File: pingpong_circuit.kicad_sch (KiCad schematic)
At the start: 10 parts, among them J1 XH, SW1 PA, SW2 PA, U1 Pico, U2 A000053

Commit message: hoge
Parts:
- added J2: Brushless, symbol Connector:Conn_01x02_Pin
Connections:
- net at U1.4 (GPIO2): now also J2.2 (Pin_2)
- net at U1.5 (GPIO3): now also J2.1 (Pin_1)
- no-connect marks 1 -> 3
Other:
- note added: "servo?"
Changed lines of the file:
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@@
 	(generator_version "9.0")
 	(paper "A4")
+	(text "servo?"
+		(exclude_from_sim no)
+		(at 100.33 61.722 0)
+		(effects
+			(font
+				(size 1.27 1.27)
+			)
+		)
+	)
 	(text "赤\n青\n緑\n黒"
 		(exclude_from_sim no)
@@
 	)
 	(no_connect
+		(at 55.88 31.75)
+	)
+	(no_connect
+		(at 55.88 41.91)
+	)
+	(no_connect
 		(at 228.6 46.99)
 	)
@@
 	(wire
 		(pts
+			(xy 92.71 52.07) (xy 92.71 66.04)
+		)
+		(stroke
+			(width 0)
+			(type default)
+		)
+	)
+	(wire
+		(pts
 			(xy 228.6 52.07) (xy 223.52 52.07)
 		)
@@
 	(wire
 		(pts
+			(xy 97.79 55.88) (xy 97.79 39.37)
+		)
+		(stroke
+			(width 0)
+			(type default)
+		)
+	)
+	(wire
+		(pts
 			(xy 132.08 80.01) (xy 123.19 80.01)
 		)
@@
 	(wire
 		(pts
+			(xy 55.88 44.45) (xy 95.25 44.45)
+		)
+		(stroke
+			(width 0)
+			(type default)
+		)
+	)
+	(wire
+		(pts
 			(xy 123.19 68.58) (xy 123.19 64.77)
 		)
@@
 	(wire
 		(pts
+			(xy 95.25 44.45) (xy 95.25 63.5)
+		)
+		(stroke
+			(width 0)
+			(type default)
+		)
+	)
+	(wire
+		(pts
 			(xy 251.46 57.15) (xy 264.16 57.15)
 		)
@@
 	(wire
 		(pts
+			(xy 100.33 53.34) (xy 109.22 53.34)
+		)
+		(stroke
+			(width 0)
+			(type default)
+		)
+	)
+	(wire
+		(pts
 			(xy 157.48 67.31) (xy 157.48 93.98)
 		)
@@
 	(wire
 		(pts
+			(xy 55.88 52.07) (xy 92.71 52.07)
+		)
+		(stroke
+			(width 0)
+			(type default)
+		)
+	)
+	(wire
+		(pts
+			(xy 95.25 63.5) (xy 100.33 63.5)
+		)
+		(stroke
+			(width 0)
+			(type default)
+		)
+	)
+	(wire
+		(pts
 			(xy 16.51 29.21) (xy 20.32 29.21)
 		)
@@
 	(wire
 		(pts
+			(xy 55.88 36.83) (xy 100.33 36.83)
+		)
+		(stroke
+			(width 0)
+			(type default)
+		)
+	)
+	(wire
+		(pts
 			(xy 219.71 62.23) (xy 228.6 62.23)
 		)
@@
 	(wire
 		(pts
+			(xy 92.71 66.04) (xy 100.33 66.04)
+		)
+		(stroke
+			(width 0)
+			(type default)
+		)
+	)
+	(wire
+		(pts
 			(xy 228.6 57.15) (xy 228.6 59.69)
 		)
@@
 	(wire
 		(pts
+			(xy 109.22 55.88) (xy 97.79 55.88)
+		)
+		(stroke
+			(width 0)
+			(type default)
+		)
+	)
+	(wire
+		(pts
 			(xy 140.97 43.18) (xy 140.97 34.29)
 		)
@@
 	(wire
 		(pts
+			(xy 100.33 36.83) (xy 100.33 53.34)
+		)
+		(stroke
+			(width 0)
+			(type default)
+		)
+	)
+	(wire
+		(pts
 			(xy 228.6 64.77) (xy 222.25 64.77)
+		)
+		(stroke
+			(width 0)
+			(type default)
+		)
+	)
+	(wire
+		(pts
+			(xy 97.79 39.37) (xy 55.88 39.37)
 		)
 		(stroke
@@
 					(unit 1)
 				)
+			)
+		)
+	)
+	(symbol
+		(lib_id "Connector:Conn_01x02_Pin")
+		(at 114.3 55.88 180)
+		(unit 1)
+		(exclude_from_sim no)
+		(in_bom yes)
+		(on_board yes)
+		(dnp no)
+		(fields_autoplaced yes)
+		(property "Reference" "J2"
+			(at 115.57 53.3399 0)
+			(effects
+				(font
+					(size 1.27 1.27)
+				)
+				(justify right)
+			)
+		)
+		(property "Value" "Brushless"
+			(at 115.57 55.8799 0)
+			(effects
+				(font
+					(size 1.27 1.27)
+				)
+				(justify right)
+			)
+		)
+		(property "Footprint" ""
+			(at 114.3 55.88 0)
+			(effects
+				(font
+					(size 1.27 1.27)
+				)
+				(hide yes)
+			)
+		)
+		(property "Datasheet" "~"
+			(at 114.3 55.88 0)
+			(effects
+				(font
+					(size 1.27 1.27)
+				)
+				(hide yes)
+			)
+		)
+		(property "Description" "Generic connector, single row, 01x02, script generated"
+			(at 114.3 55.88 0)
+			(effects
+				(font
+					(size 1.27 1.27)
+				)
+				(hide yes)
+			)
+		)
+		(pin "1"
+		)
+		(pin "2"
+		)
+		(instances
+			(project ""
+				(path "/fc07d479-f2e9-4808-b332-bbe7c10248ce"
+					(reference "J2")
+					(unit 1)
+				)

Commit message: 一旦全体像把握
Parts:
- removed J2: Brushless, symbol Connector:Conn_01x02_Pin
- added C3: 470u, symbol Device:C_Polarized
- added C4, C5: C_Polarized, symbol Device:C_Polarized
- added J10: QI_3, symbol Connector:Conn_01x03_Pin
- added J2: QI_Servo_Roll, symbol Connector:Conn_01x03_Pin
- added J3: QI_Blushless_Left, symbol Connector:Conn_01x03_Pin
- added J4: QI_Blushless_Right, symbol Connector:Conn_01x03_Pin
- added J5: QI_Servo_Pitch, symbol Connector:Conn_01x03_Pin
- added J6: QI_Servo_Yaw, symbol Connector:Conn_01x03_Pin
- added J7: QI_Servo_Loading, symbol Connector:Conn_01x03_Pin
- added J8: Arduino_Uno_UART, symbol Connector:Conn_01x04_Pin
- added J9: XT60, symbol Connector_Generic:Conn_01x02
- U3: value ~ -> A4988
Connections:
- net +5V: now also J8.4 (Pin_4)
- net GND: now also U1.13 (GND), U1.18 (GND), U1.23 (GND), U1.28 (GND), U1.33 (AGND), U1.38 (GND), U1.8 (GND), C3.2, C4.2, C5.2, J10.2 (Pin_2), J2.1 (Pin_1), J3.1 (Pin_1), J4.1 (Pin_1), J5.1 (Pin_1), J6.1 (Pin_1), J7.1 (Pin_1), J8.1 (Pin_1), J9.1 (Pin_1); no longer U3.2 (MS1), U3.3 (MS2), U3.4 (MS3)
- net at U3.1 (~{ENABLE}): now also U2.12 (7)
- net at U3.5 (~{RESET}), U3.6 (~{SLEEP}): now also U2.18 (13(PWM))
- net at U2.15 (10(PWM)/A10): now also U3.2 (MS1)
- net at U2.16 (11(PWM)): now also U3.3 (MS2)
- net at U2.17 (12/A11): now also U3.4 (MS3)
- net at U2.3 (1/TX): now also U1.21 (GPIO16)
- net at U2.4 (0/RX): now also U1.22 (GPIO17); no longer U1.1 (GPIO0)
- net at U1.5 (GPIO3): now also J5.3 (Pin_3)
- net at U1.4 (GPIO2): now also J2.3 (Pin_3)
- net at U1.15 (GPIO11): now also J8.3 (Pin_3)
- net at U1.16 (GPIO12): now also J8.2 (Pin_2)
- net at U1.2 (GPIO1): now also J4.3 (Pin_3)
- net at U1.7 (GPIO5): now also J6.3 (Pin_3)
- net at U1.9 (GPIO6): now also J7.3 (Pin_3)
- net +24V renamed +15V
- net +15V: now also C3.1, C4.1, J9.2 (Pin_2)
- new net: J3.3 (Pin_3), U1.1 (GPIO0)
- new net +7.5V: C5.1, J10.1 (Pin_1), J2.2 (Pin_2), J5.2 (Pin_2), J6.2 (Pin_2), J7.2 (Pin_2)
- no-connect marks 3 -> 44
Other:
- note removed: "servo?"
- moved on the sheet: C1, C2, J1, R1, R2, SW1, SW2, U1, U2, U3

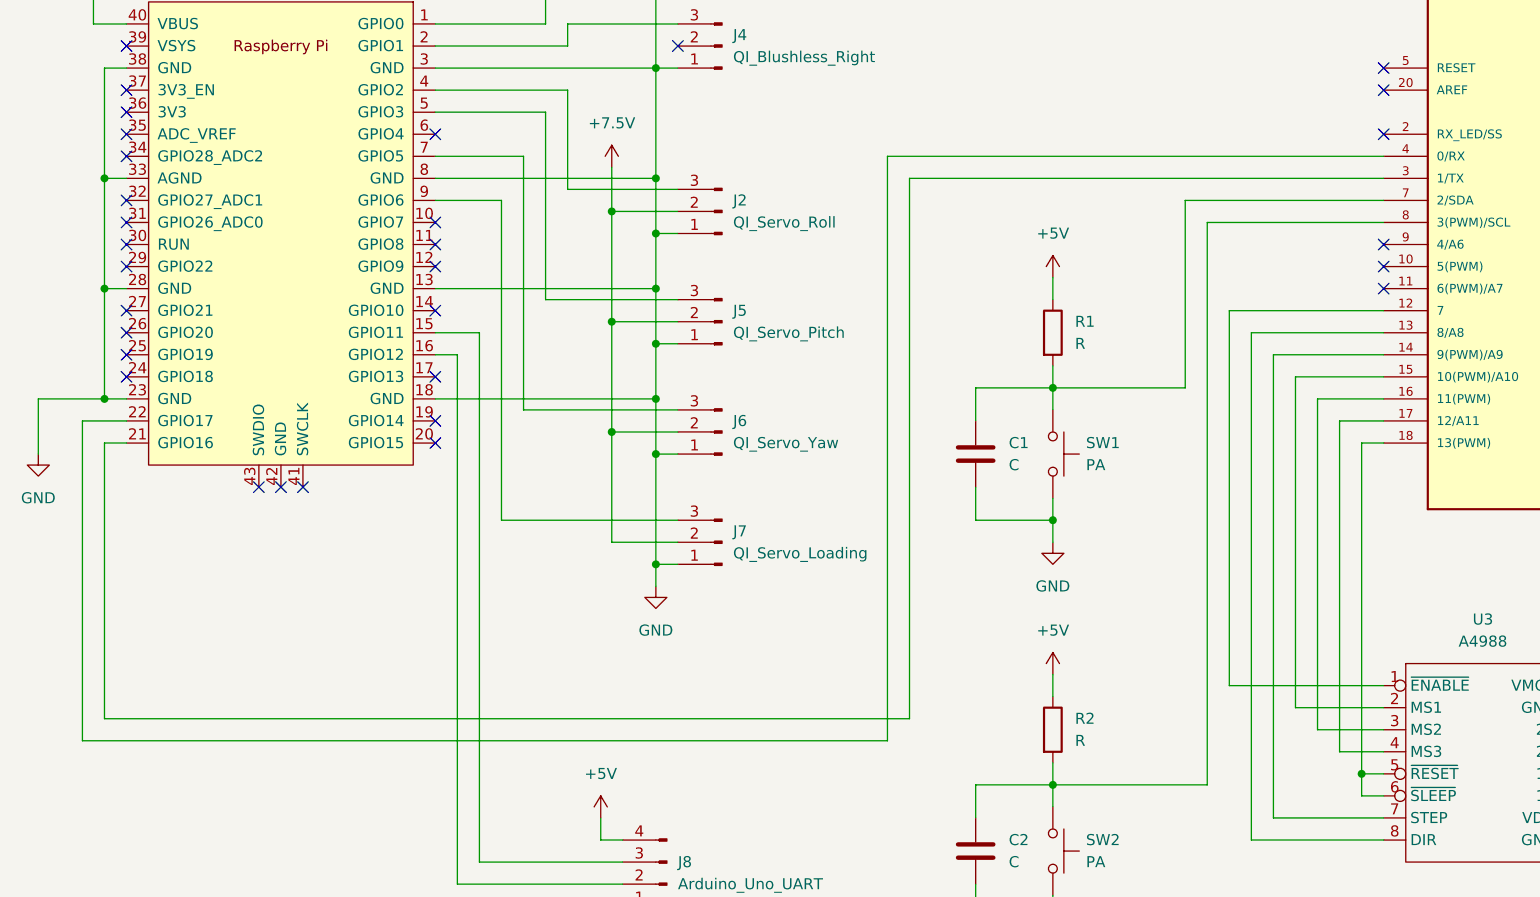
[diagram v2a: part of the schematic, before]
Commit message: tx rx 逆だった
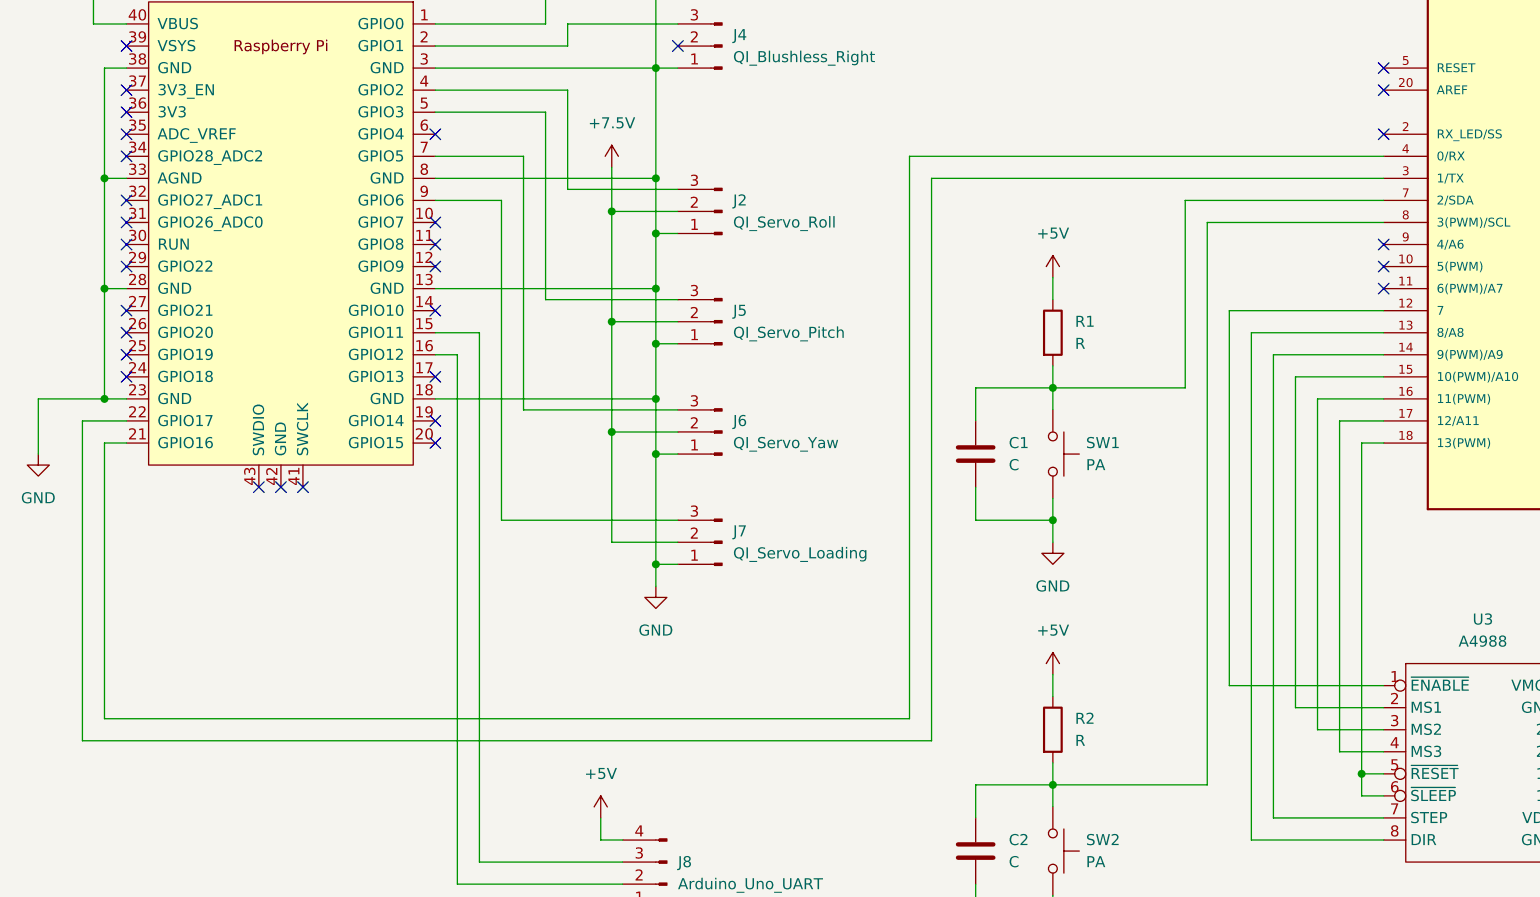
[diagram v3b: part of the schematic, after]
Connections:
- net at U2.3 (1/TX): now also U1.22 (GPIO17); no longer U1.21 (GPIO16)
- net at U2.4 (0/RX): now also U1.21 (GPIO16); no longer U1.22 (GPIO17)
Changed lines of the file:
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@@
+	(wire
+		(pts
+			(xy 116.84 44.45) (xy 171.45 44.45)
+		)
+		(stroke
+			(width 0)
+			(type default)
+		)
+	)
 	(wire
 		(pts
@@
 	(wire
 		(pts
+			(xy 119.38 46.99) (xy 171.45 46.99)
+		)
+		(stroke
+			(width 0)
+			(type default)
+		)
+	)
+	(wire
+		(pts
 			(xy 107.95 151.13) (xy 107.95 153.67)
 		)
@@
 	(wire
 		(pts
-			(xy 116.84 109.22) (xy 116.84 46.99)
-		)
-		(stroke
-			(width 0)
-			(type default)
-		)
-	)
-	(wire
-		(pts
 			(xy 171.45 72.39) (xy 163.83 72.39)
 		)
@@
 	(wire
 		(pts
-			(xy 116.84 46.99) (xy 171.45 46.99)
-		)
-		(stroke
-			(width 0)
-			(type default)
-		)
-	)
-	(wire
-		(pts
 			(xy 62.23 46.99) (xy 87.63 46.99)
 		)
@@
 	(wire
 		(pts
+			(xy 119.38 111.76) (xy 119.38 46.99)
+		)
+		(stroke
+			(width 0)
+			(type default)
+		)
+	)
+	(wire
+		(pts
 			(xy 87.63 66.04) (xy 90.17 66.04)
 		)
@@
 	(wire
 		(pts
-			(xy 114.3 44.45) (xy 171.45 44.45)
-		)
-		(stroke
-			(width 0)
-			(type default)
-		)
-	)
-	(wire
-		(pts
 			(xy 194.31 107.95) (xy 196.85 107.95)
 		)
@@
 	(wire
 		(pts
+			(xy 116.84 44.45) (xy 116.84 109.22)
+		)
+		(stroke
+			(width 0)
+			(type default)
+		)
+	)
+	(wire
+		(pts
 			(xy 87.63 91.44) (xy 87.63 93.98)
 		)
@@
 	(wire
 		(pts
-			(xy 114.3 44.45) (xy 114.3 111.76)
-		)
-		(stroke
-			(width 0)
-			(type default)
-		)
-	)
-	(wire
-		(pts
 			(xy 24.13 59.69) (xy 24.13 46.99)
 		)
@@
 	(wire
 		(pts
-			(xy 21.59 111.76) (xy 114.3 111.76)
-		)
-		(stroke
+			(xy 21.59 111.76) (xy 119.38 111.76)
+		)
+		(stroke

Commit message: 回路図整理
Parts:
- added J11: QI_GP4, symbol Connector:Conn_01x03_Pin
- added J12: QI_GP6, symbol Connector:Conn_01x03_Pin
- added J13: QI_GP8, symbol Connector:Conn_01x03_Pin
- added J14: QI_GP9, symbol Connector:Conn_01x03_Pin
- C1, C2: value C -> 0.1u
- C4, C5: value C_Polarized -> 47u
- J2: value QI_Servo_Roll -> QI_GP2
- J5: value QI_Servo_Pitch -> QI_GP3
- J6: value QI_Servo_Yaw -> QI_GP5
- J7: value QI_Servo_Loading -> QI_GP7
- R1, R2: value R -> 100k
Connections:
- net +7.5V: now also J11.2 (Pin_2), J12.2 (Pin_2), J13.2 (Pin_2), J14.2 (Pin_2)
- net GND: no longer J2.1 (Pin_1), J3.1 (Pin_1), J4.1 (Pin_1), J5.1 (Pin_1), J6.1 (Pin_1), J7.1 (Pin_1), U1.13 (GND), U1.18 (GND), U1.3 (GND), U1.8 (GND)
- net at U1.9 (GPIO6): now also J12.3 (Pin_3); no longer J7.3 (Pin_3)
- net at J8.2 (Pin_2): now also U1.15 (GPIO11); no longer U1.16 (GPIO12)
- net at J8.3 (Pin_3): now also U1.16 (GPIO12); no longer U1.15 (GPIO11)
- net at U1.10 (GPIO7): now also J7.3 (Pin_3)
- net at U1.11 (GPIO8): now also J13.3 (Pin_3)
- net at U1.12 (GPIO9): now also J14.3 (Pin_3)
- net at U1.6 (GPIO4): now also J11.3 (Pin_3)
- new net: J11.1 (Pin_1), J12.1 (Pin_1), J13.1 (Pin_1), J14.1 (Pin_1), J2.1 (Pin_1), J3.1 (Pin_1), J4.1 (Pin_1), J5.1 (Pin_1), J6.1 (Pin_1), J7.1 (Pin_1), U1.13 (GND), U1.3 (GND), U1.8 (GND)
- no-connect marks 44 -> 40
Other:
- note added: "RX"
- note added: "TX"
- note added: "サーボ電源"
- note added: "ブラシレス＆ステッピング電源"
- moved on the sheet: C3, C4, C5, J1, J10, J2, J3, J4, J5, J6, J7, J8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
